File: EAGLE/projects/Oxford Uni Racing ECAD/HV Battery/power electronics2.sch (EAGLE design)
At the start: 35 parts, among them IC1 4043N, IC2 4001N, IC3 LM555CN, IC4 4071N, K1 T9AS1D12-48=T9A, K2 T9AS5D12-12=T9A, K4 T9AS1D12-48=T9A, K5 T9AS1D12-48=T9A, Q1 BSS92, Q2 BSS92

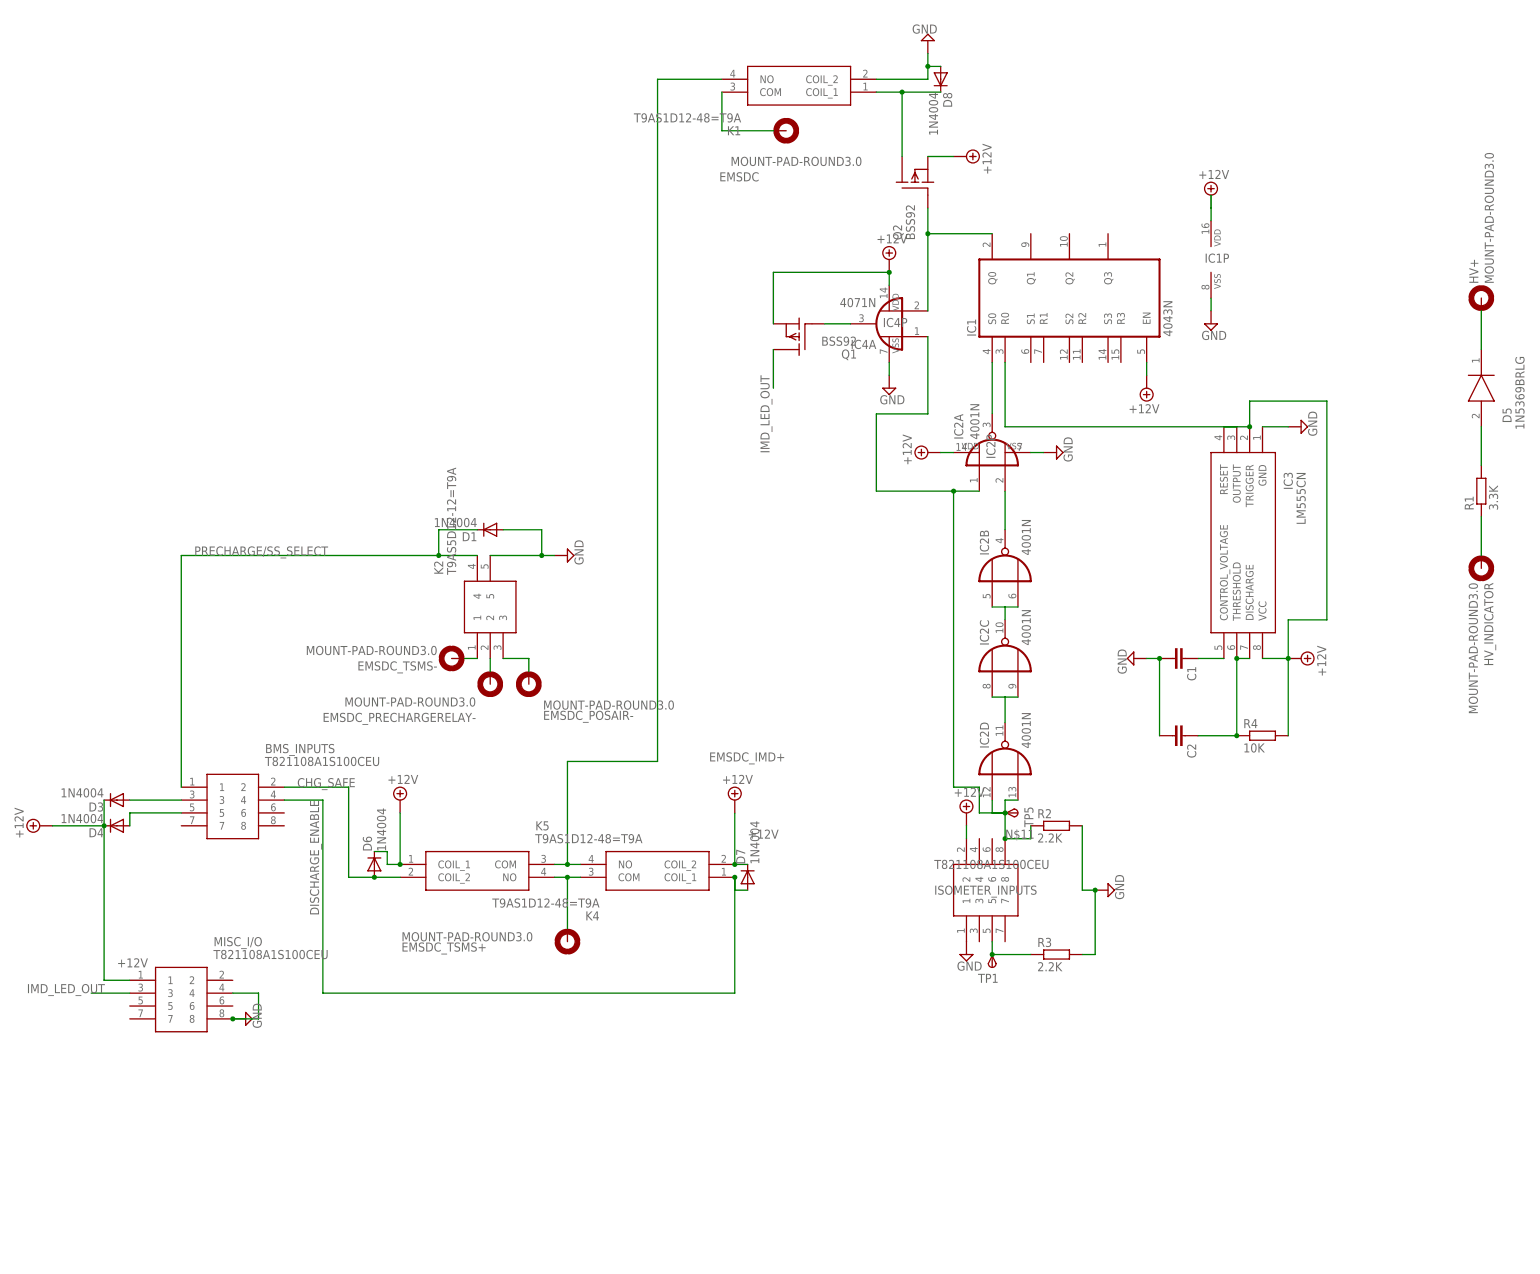
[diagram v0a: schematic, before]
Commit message: Added positive edge detection for ams relays and leds
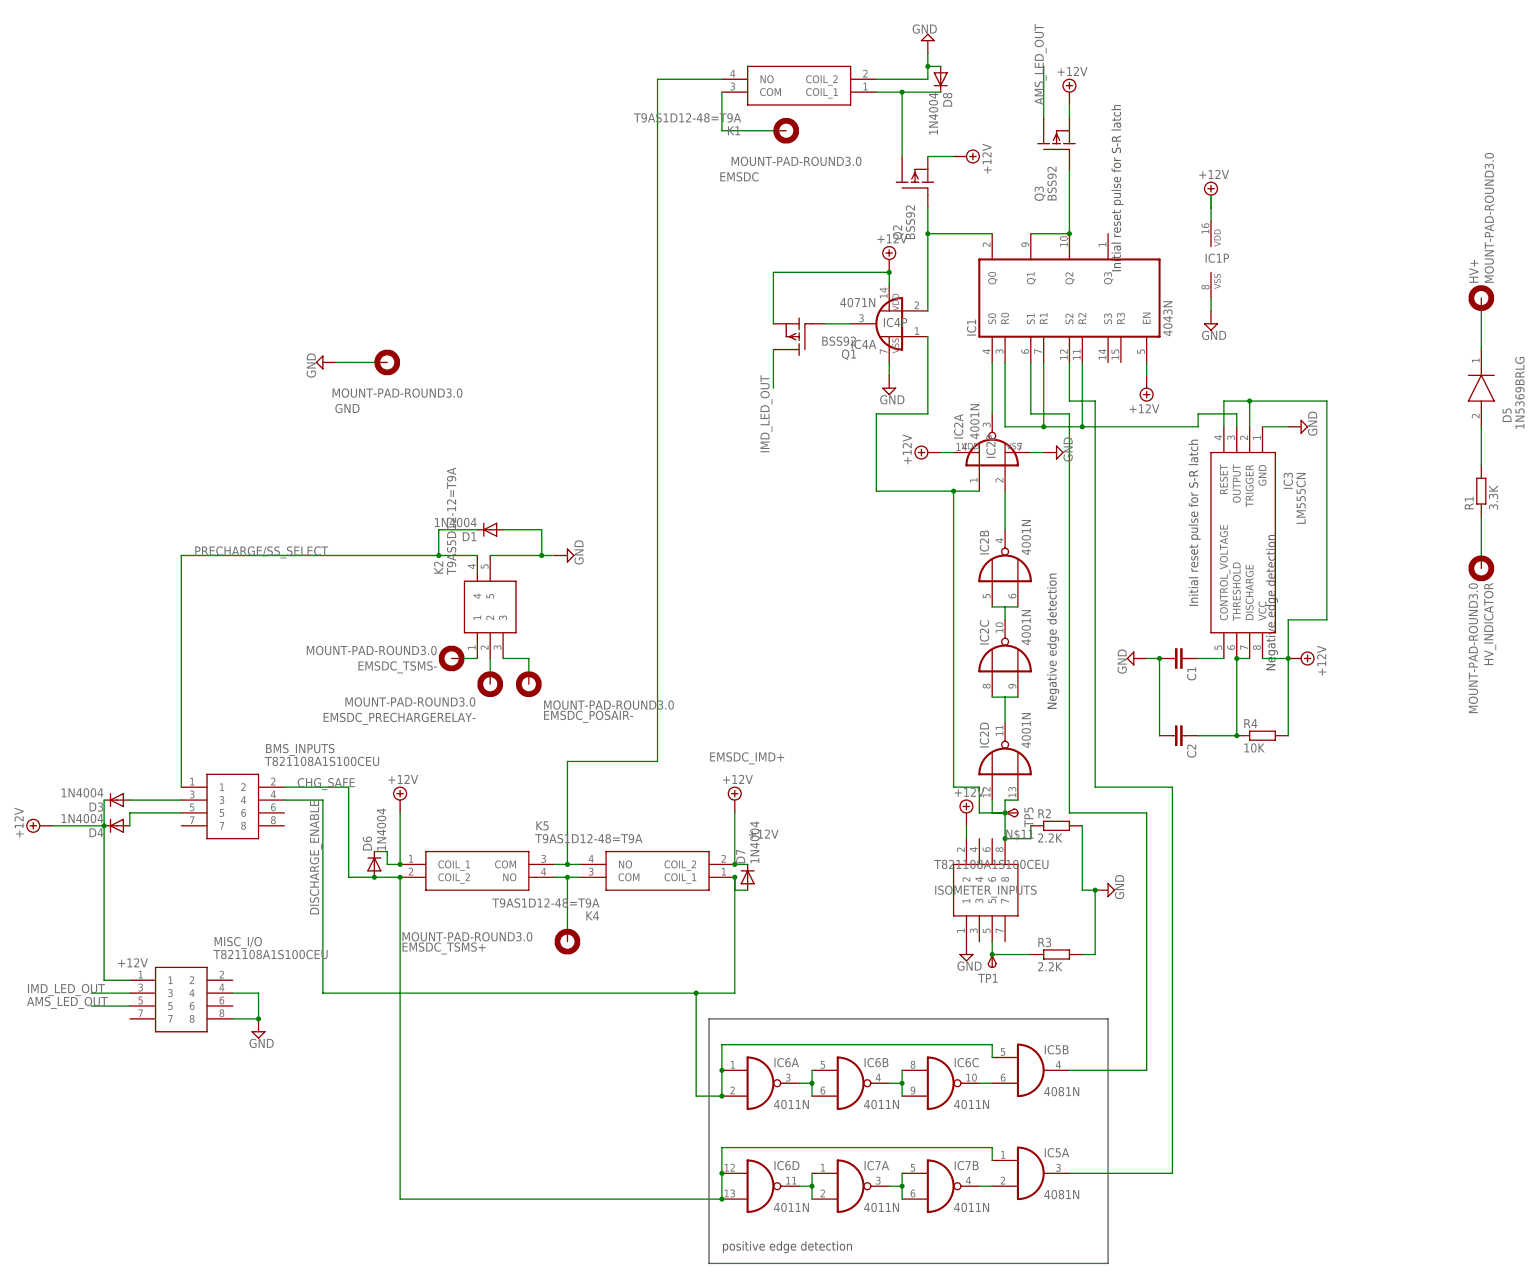
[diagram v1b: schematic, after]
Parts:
- added GND: MOUNT-PAD-ROUND3.0, holes:MOUNT-PAD-ROUND3.0
- added IC5: 4081N, 40xx:4081N
- added IC6, IC7: 4011N, 40xx:4011N
- added Q3: BSS92, transistor-fet:BSS92
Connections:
- new net AMS_LED_OUT: MISC_I/O.5, Q3.D
- new net N$23: IC1A.S1, IC5B.O
- new net N$24: IC6A.O, IC6B.I0, IC6B.I1
- new net N$25: IC6B.O, IC6C.I0, IC6C.I1
- new net N$26: IC5B.I1, IC6C.O
- new net N$27: IC1A.S2, IC5A.O
- new net N$28: IC5A.I1, IC7B.O
- new net N$29: IC1A.Q1, IC1A.Q2, Q3.G
- new net N$30: IC7A.O, IC7B.I0, IC7B.I1
- new net N$32: IC6D.O, IC7A.I0, IC7A.I1
- net +12V: now also Q3.S
- net CHG_SAFE: now also IC5A.I0, IC6D.I0, IC6D.I1
- net DISCHARGE_ENABLE: now also IC5B.I0, IC6A.I0, IC6A.I1
- net GND: now also GND.MOUNT
- net N$20: now also IC1A.R1, IC1A.R2
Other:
- note added: "Initial reset pulse for S-R latch"
- note added: "Negative edge detection"
- note added: "positive edge detection"
